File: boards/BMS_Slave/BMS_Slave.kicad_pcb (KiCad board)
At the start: 4 copper layers, 155 x 75 mm, 133 parts, among them J1 Mounting_Hole_4-40, J2 Mounting_Hole_4-40, J3 Mounting_Hole_4-40, J4 Mounting_Hole_4-40, J5 MicroFit_12, J6 MicroFit_20, J7 NanoFit_2, J8 NanoFit_2, Q1 Q_NPN_BCE, Q10 NMOS_GSD_30V, Q11 NMOS_GSD_30V, Q2 NMOS_GSD_30V, Q3 NMOS_GSD_30V, Q4 NMOS_GSD_30V, Q5 NMOS_GSD_30V, Q6 NMOS_GSD_30V, Q7 NMOS_GSD_30V, Q8 NMOS_GSD_30V, Q9 NMOS_GSD_30V, T1 T_LAN_7490100111A, U1 LTC6811-1, U2 24AA01, U3 MCP6001, U4 LTC1380, U5 LTC1380, U6 MCP6001

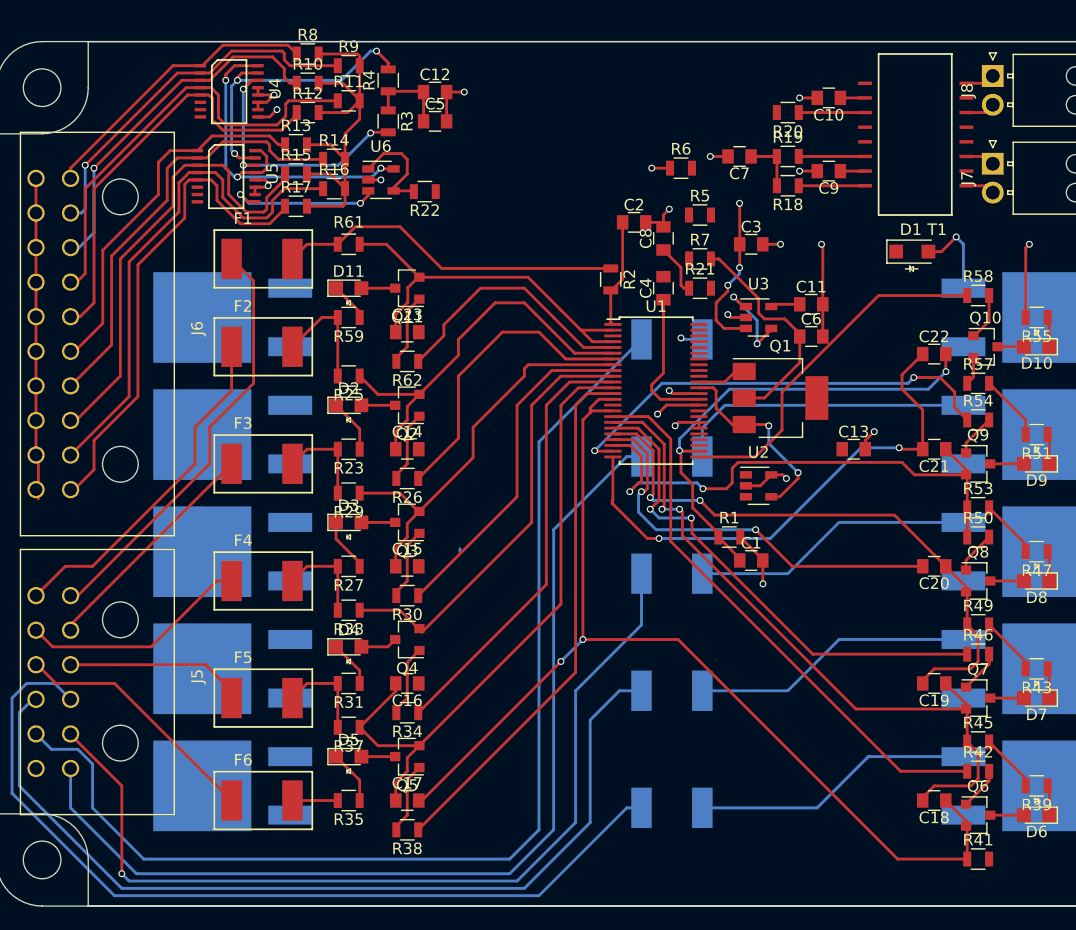
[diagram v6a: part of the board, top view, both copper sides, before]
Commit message: BMS Slave: completed tracing and layout
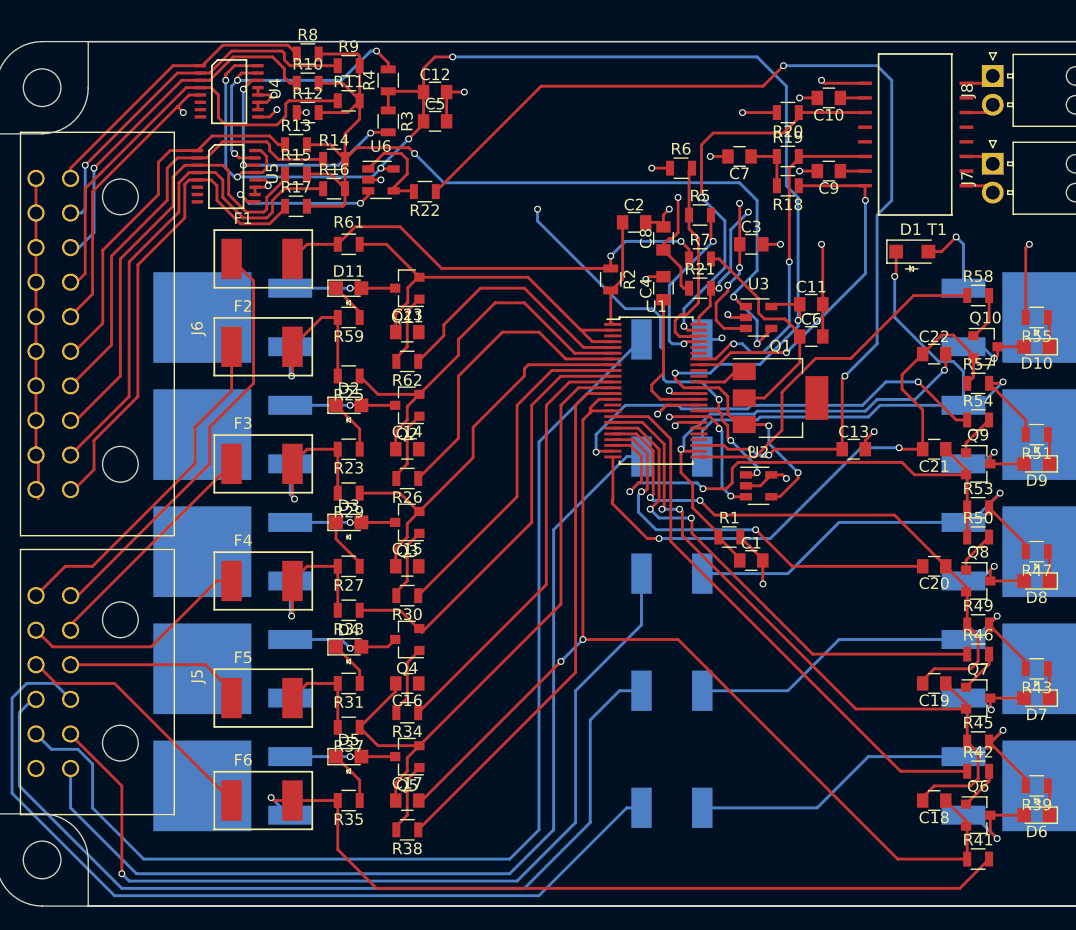
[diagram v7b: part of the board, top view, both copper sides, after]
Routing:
- net /GPIO1: track 0.00 -> 91.4 mm, vias 0 -> 4
- net /VREG: track 58.3 -> 136.9 mm, vias 5 -> 9
- net /Balance6/V_BELOW: track 3.93 -> 71.4 mm, vias 0 -> 1
- net /SCL: track 25.9 -> 85.8 mm, vias 3 -> 7
- net /SDA: track 23.0 -> 80.8 mm, vias 3 -> 6
- net /VREF2: track 44.4 -> 91.7 mm, vias 2 -> 3
- net Net-(R21-Pad2): track 0.00 -> 30.8 mm, vias 0 -> 3
- net Net-(R20-Pad1): track 5.74 -> 35.1 mm, vias 0 -> 2
- net Net-(R18-Pad1): track 5.74 -> 31.1 mm, vias 0 -> 2
- net Net-(R19-Pad2): track 5.74 -> 30.5 mm, vias 0 -> 2
- net /Balance2/V_BELOW: track 31.7 -> 53.7 mm, vias 0 -> 2
- net Net-(R5-Pad1): track 0.00 -> 18.1 mm
- net Net-(C8-Pad1): track 4.50 -> 22.4 mm, vias 0 -> 2
- net Net-(R5-Pad2): track 0.00 -> 15.3 mm, vias 0 -> 2
- net /Balance10/V_CELL: track 30.3 -> 39.8 mm, vias 0 -> 2
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- added copper zone on In2.Cu, net (none)

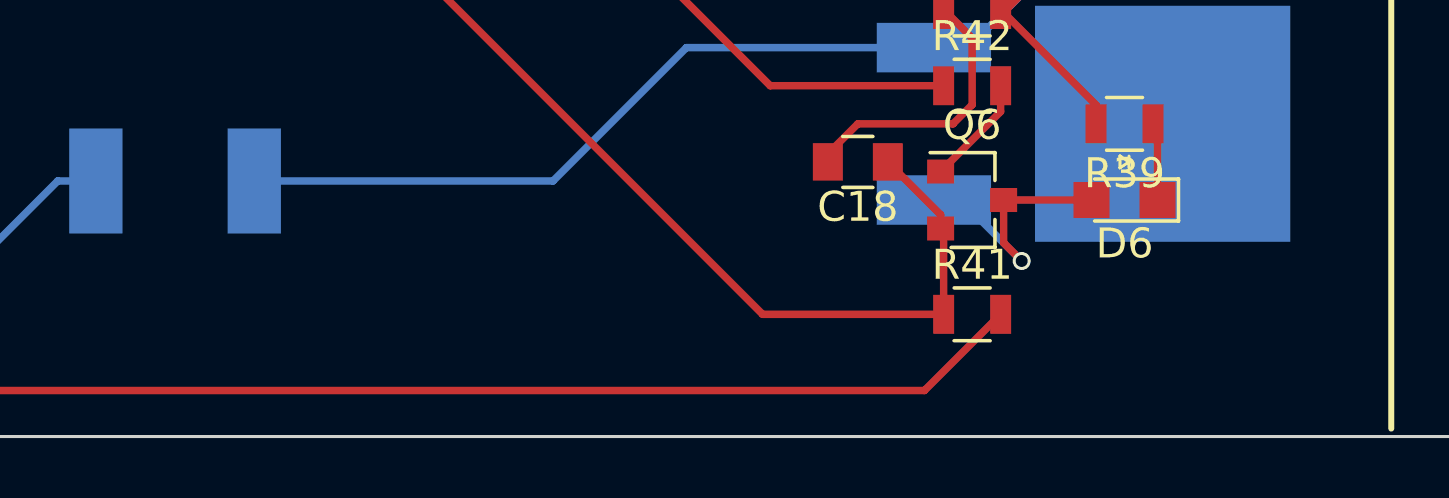
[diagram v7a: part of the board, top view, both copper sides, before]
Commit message: BMS SLave: added text
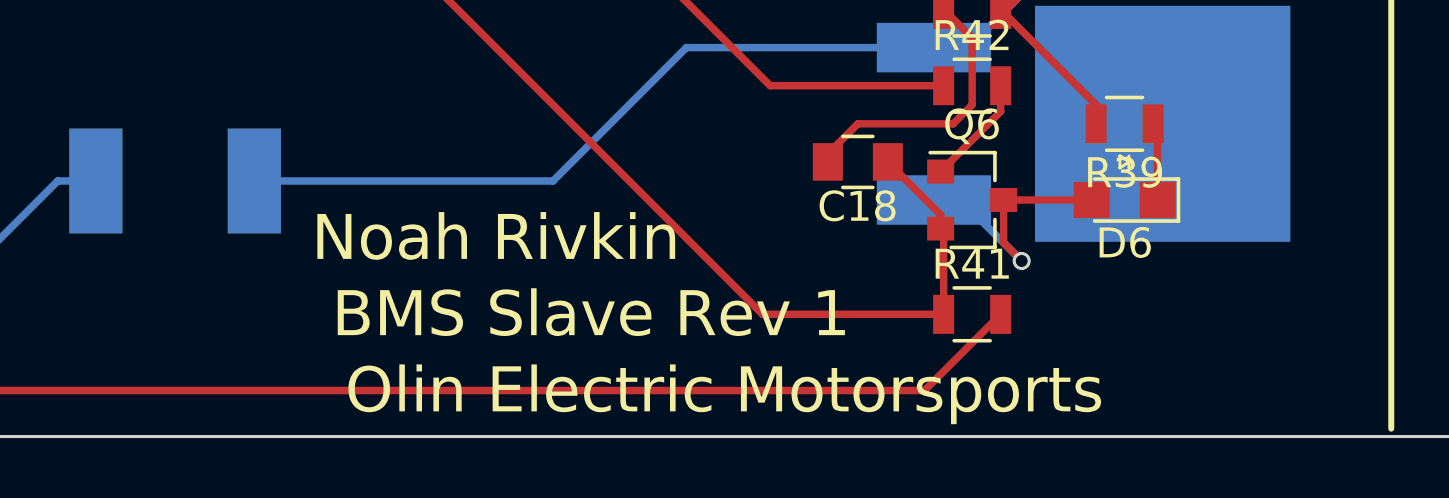
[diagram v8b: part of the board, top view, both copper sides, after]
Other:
- board text added: "BMS Slave Rev 1"
- board text added: "Noah Rivkin"
- board text added: "Olin Electric Motorsports"
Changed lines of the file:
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@@
     (area 60.198 50.038 267.627769 170.434001)
     (thickness 1.6)
-    (drawings 32)
+    (drawings 34)
     (tracks 1154)
     (zones 0)
@@
     (0 F.Cu signal)
     (1 In1.Cu signal hide)
-    (2 In2.Cu signal)
+    (2 In2.Cu signal hide)
     (31 B.Cu signal)
     (32 B.Adhes user)
@@
     )
   )
-  (gr_line (start 126.111 142.494) (end 126.111 68.834) (angle 90) (layer B.Mask) (width 0.2))
+  (gr_text "Noah Rivkin\n" (at 140.335 135.89) (layer F.SilkS)
+    (effects (font (size 1.5 1.5) (thickness 0.3)))
+  )
+  (gr_text "Olin Electric Motorsports" (at 147.955 140.97) (layer F.SilkS)
+    (effects (font (size 1.5 1.5) (thickness 0.3)))
+  )
+  (gr_text "BMS Slave Rev 1" (at 143.51 138.43) (layer F.SilkS)
+    (effects (font (size 1.5 1.5) (thickness 0.3)))
+  )
   (gr_arc (start 75.0011 138.5036) (end 79.0011 138.5036) (angle -90) (layer Edge.Cuts) (width 0.1))
   (gr_line (start 79.0011 142.5036) (end 79.0011 138.5036) (layer Edge.Cuts) (width 0.1))
